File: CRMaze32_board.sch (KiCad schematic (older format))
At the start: 113 parts, among them IC101 L298, P101 CONN_01X02, P102 CONN_01X06, P103 CONN_01X06, P104 CONN_01X02, Q101 BFR92, Q102 BFR92, Q103 BFR92, Q104 BFR92, Q105 BFR92, SW101 SWITCH_INV, U101 LD1117S50TR, U102 74AHC1G14, U103 74AHC1G14, U104 LD1117S33TR, U105 ESP32-WROOM

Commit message: Placa CRMaze_board_futura con forma y componente colocados
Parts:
- removed 47K101, 47K102, 47K103, 47K104, 47K105, R105, R106, R110, R111, R114, R115, R? (x3): R, symbol R
- removed C101: 100n, symbol C
- removed C102: 10u, symbol C
- removed C103: 100n, Capacitors_SMD:C_0805_HandSoldering, symbol C
- removed C104: 10u, Capacitors_SMD:C_1206, symbol C
- removed D102, D107, D115, D116, D119, D120, D121, D122, D? (x3): LED, symbol LED
- removed D103, D104, D105, D106, D108, D109, D110, D111: D, diodos_smd:SMD_D_SMA-Sub-2, symbol D_Schottky
- removed IC101: L298, TO_SOT_Packages_THT:Multiwatt_15_Vertical, symbol L298
- removed P101: CONN_01X02, Pin_Headers:Pin_Header_Angled_1x02, symbol CONN_01X02
- removed P102, P103: CONN_01X06, Pin_Headers:Pin_Header_Straight_1x06, symbol CONN_01X06
- removed Q101, Q102, Q103, Q104, Q105: BFR92, symbol BFR92
- removed R101: 20k, symbol R
- removed R102: 10k, symbol R
- removed R103, R104: 0.5, Resistors_SMD:R_1206, symbol R
- removed SW101: SWITCH_INV, Buttons_Switches_SMD:SW_DIP_x4_W5.9mm_Slide_Copal_CVS, symbol SWITCH_INV
- removed U101: LD1117S50TR, symbol LD1117S50TR
- removed U102, U103: 74AHC1G14, symbol 74AHC1G14
- removed U104: LD1117S33TR, TO_SOT_Packages_SMD:SOT-223, symbol LD1117S33TR
- removed U?: ADXRS620_breakout, symbol ADXRS620_breakout
- removed U?: DRV8825_pololu, symbol DRV8825_pololu
- added J101, J102: CONN_01X02, Pin_Headers:Pin_Header_Angled_1x02, symbol CONN_01X02
- added P101: GYRO_ADXRS_2, Pin_Headers:Pin_Header_Straight_1x05, symbol CONN_01X05
- added P102: GYRO_ADXRS_1, Pin_Headers:Pin_Header_Straight_1x03, symbol CONN_01X03
- added P103: SERIAL, Pin_Headers:Pin_Header_Straight_1x03, symbol CONN_01X03
- added P105: ENC_1_POWER, Pin_Headers:Pin_Header_Straight_1x02, symbol CONN_01X02
- added P106: ENC_2_IN, Pin_Headers:Pin_Header_Straight_1x02, symbol CONN_01X02
- added P107: ENC_2_POWER, Pin_Headers:Pin_Header_Straight_1x02, symbol CONN_01X02
- added P108: MOTOR1, Pin_Headers:Pin_Header_Straight_1x02, symbol CONN_01X02
- added P109: MOTOR2, Pin_Headers:Pin_Header_Straight_1x02, symbol CONN_01X02
- added SW101: EN, Buttons_Switches_SMD:SW_SPST_EVQQ2, symbol SW_PUSH-RESCUE-CRMaze32_board
- added SW102: PUSH_IO_0, Buttons_Switches_SMD:SW_SPST_EVQQ2, symbol SW_PUSH-RESCUE-CRMaze32_board
- added SW103: SW_SPDT, switch:switch_power_custom, symbol SW_SPDT
- added U105: DRV8835_pololu, Housings_DIP:DIP-14_W7.62mm, symbol DRV8835_pololu
- 1.8k101: renamed from R107; footprint (none) -> Resistors_SMD:R_0805
- 1.8k102: renamed from R108; footprint (none) -> Resistors_SMD:R_0805
- 1.8k103: renamed from R109; footprint (none) -> Resistors_SMD:R_0805
- 1.8k104: renamed from R112; footprint (none) -> Resistors_SMD:R_0805
- 1.8k105: renamed from R113; footprint (none) -> Resistors_SMD:R_0805
- 1.8k106: renamed from R116; footprint (none) -> Resistors_SMD:R_0805
- 10ohm101, 10ohm102, 2.8ohm101, 2.8ohm102: renamed from R?; footprint (none) -> Resistors_SMD:R_1206
- 10uH101: renamed from 10uH; footprint (none) -> Capacitors_SMD:C_1206; symbol INDUCTOR -> INDUCTOR-RESCUE-CRMaze32_board
- 1k101, 1k102, 1k103, 1k104: renamed from R?; footprint (none) -> Resistors_SMD:R_0805
- BZ101: footprint (none) -> Capacitors_SMD:c_elec_4x5.8
- C101: renamed from C?; value C -> 100n; footprint (none) -> Capacitors_SMD:C_0805
- C102: renamed from C?; value C -> 10u; footprint (none) -> Capacitors_SMD:C_1206
- C103, C105, C108: renamed from C?; footprint (none) -> Capacitors_SMD:C_1206
- C104, C106, C107, C109: renamed from C?; footprint (none) -> Capacitors_SMD:C_0805
- C110, C112, C114: renamed from C?; value C -> 4.7uF; footprint (none) -> Capacitors_SMD:C_1206
- C111, C113, C115: renamed from C?; value C -> 100nF; footprint (none) -> Capacitors_SMD:C_0805
- D101, D114, D115, D116: renamed from D?; footprint (none) -> LEDs:LED-3MM; symbol LED -> LED-RESCUE-CRMaze32_board
- D102: renamed from D101; footprint (none) -> Diodes_SMD:D_0805
- D103: renamed from D112; value LED -> IR_DET; footprint (none) -> LEDs:LED-3MM; symbol LED -> LED-RESCUE-CRMaze32_board
- D104: renamed from D113; value LED -> IR_DET; footprint (none) -> LEDs:LED-3MM; symbol LED -> LED-RESCUE-CRMaze32_board
- D105, D107, D109, D110, D112, D113: renamed from D?; value LED -> IR_EMM; footprint (none) -> LEDs:LED-3MM; symbol LED -> LED-RESCUE-CRMaze32_board
- D106: renamed from D114; value LED -> IR_DET; footprint (none) -> LEDs:LED-3MM; symbol LED -> LED-RESCUE-CRMaze32_board
- D108: renamed from D117; value LED -> IR_DET; footprint (none) -> LEDs:LED-3MM; symbol LED -> LED-RESCUE-CRMaze32_board
- D111: renamed from D118; value LED -> IR_DET; footprint (none) -> LEDs:LED-3MM; symbol LED -> LED-RESCUE-CRMaze32_board
- D120: renamed from D123; value LED -> IR_DET; footprint (none) -> LEDs:LED-3MM; symbol LED -> LED-RESCUE-CRMaze32_board
- L101, L102, L103: renamed from L?; footprint (none) -> Capacitors_SMD:C_1206; symbol INDUCTOR -> INDUCTOR-RESCUE-CRMaze32_board
- P104: value CONN_01X02 -> ENC_1_IN; footprint Pin_Headers:Pin_Header_Angled_1x02 -> Pin_Headers:Pin_Header_Straight_1x02
- U102: renamed from U?; footprint (none) -> Housings_SOIC:SOIC-8-1EP_3.9x4.9mm_Pitch1.27mm
- U103: renamed from U?; footprint (none) -> TO_SOT_Packages_SMD:SOT-23-5
- U104: renamed from U?; footprint (none) -> Housings_SSOP:TSSOP-16_4.4x5mm_Pitch0.65mm; symbol ULN2003A -> ULN2003A-RESCUE-CRMaze32_board
- renumbered U105 to U101
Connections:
- net labels added: ENC_1_A, ENC_1_B, ENC_2_A, ENC_2_B
- net labels removed: +3.3V, +5V, CURRENT1, CURRENT2, ENC1_A, ENC1_B, ENC2_A, ENC2_B, GPIO_IR1, GPIO_IR23, GPIO_IR45, GPIO_IR6, GPIO_LED4, GPIO_LED5, GPIO_LED6, M1+, M1-, M2+, M2-, VCC, VDD, VOL_BAT
- wire segments 162 -> 147
- no-connect marks 3 -> 6
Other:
- note added: "ENCODERS"
- note removed: "A) LED IR EMMITER SYSTEM"
- note removed: "A) MOTOR DRIVER\n"
- note removed: "A) POWER SYSTEM CRMaze"
- moved on the sheet: 1.8k101, 1.8k102, 1.8k103, 1.8k104, 1.8k105, 1.8k106, 1k102, 1k103, 1k104, BZ101, C101, C102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

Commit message: retoques y moificaciones
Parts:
- removed P101: GYRO_ADXRS_2, Pin_Headers:Pin_Header_Straight_1x05, symbol CONN_01X05
- added J103: GYRO_ADXRS_2, Pin_Headers:Pin_Header_Straight_1x06, symbol CONN_01X06
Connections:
- wire segments 147 -> 145
- no-connect marks 6 -> 7
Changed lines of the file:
@@
 Text GLabel 2750 9250 1    60   Input ~ 0
 VA3.3
-Text GLabel 1650 10350 0    60   Input ~ 0
+Text GLabel 1600 10250 0    60   Input ~ 0
 GND
 Text GLabel 1900 9850 0    60   Input ~ 0
@@
 Text GLabel 5000 5150 3    60   Input ~ 0
 GPIO_LED1
+Text GLabel 5550 3450 2    60   Input ~ 0
+M1_EN
 Text GLabel 5550 3350 2    60   Input ~ 0
-M1_EN
-Text GLabel 5550 3450 2    60   Input ~ 0
 M1_DIR
 Text GLabel 5550 3750 2    60   Input ~ 0
@@
 	11350 2650 15650 2650
 Wire Wire Line
-	1750 10300 1950 10300
-Wire Wire Line
-	1750 10300 1750 10450
-Wire Wire Line
-	1750 10450 2050 10450
-Wire Wire Line
-	1650 10350 1750 10350
-Connection ~ 1750 10350
+	1700 10200 2150 10200
+Wire Wire Line
+	1700 10200 1700 10350
+Wire Wire Line
+	1700 10350 2000 10350
+Wire Wire Line
+	1600 10250 1700 10250
+Connection ~ 1700 10250
 Wire Notes Line
 	3700 10800 1200 10800
@@
 	0    1    1    0
 $EndComp
-$Comp
-L CONN_01X05 P101
-U 1 1 592C8D5B
-P 2350 10000
-F 0 "P101" H 2350 10300 50  0000 C CNN
-F 1 "GYRO_ADXRS_2" V 2450 10000 50  0000 C CNN
-F 2 "Pin_Headers:Pin_Header_Straight_1x05" H 2350 10000 50  0001 C CNN
-F 3 "" H 2350 10000 50  0000 C CNN
-	1    2350 10000
-	1    0    0    -1
-$EndComp
 Wire Wire Line
 	2150 9800 2050 9800
@@
 Wire Wire Line
 	1900 10000 2150 10000
-Wire Wire Line
-	1950 10300 1950 10100
-Wire Wire Line
-	1950 10100 2150 10100
-Wire Wire Line
-	2150 10200 2050 10200
-Wire Wire Line
-	2050 10200 2050 10450
 Wire Wire Line
 	2500 9250 2600 9250
@@
 Wire Wire Line
 	15400 3350 15400 3250
+$Comp
+L CONN_01X06 J103
+U 1 1 593738C8
+P 2350 10050
+F 0 "J103" H 2350 10400 50  0000 C CNN
+F 1 "GYRO_ADXRS_2" V 2450 10050 50  0000 C CNN
+F 2 "Pin_Headers:Pin_Header_Straight_1x06" H 2350 10050 50  0001 C CNN
+F 3 "" H 2350 10050 50  0001 C CNN
+	1    2350 10050
+	1    0    0    -1
+$EndComp
+Wire Wire Line
+	2150 10300 2000 10300
+Wire Wire Line
+	2000 10300 2000 10350
+NoConn ~ 2150 10100
 $EndSCHEMATC

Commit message: esquematico finalizado. Componentes colocados. Comienzo del enrutado.
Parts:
- removed U104: ULN2003A, Housings_SSOP:TSSOP-16_4.4x5mm_Pitch0.65mm, symbol ULN2003A-RESCUE-CRMaze32_board
- added 10ohm103, 10ohm104, R101, R102, R103, R104, R105, R106, R107: R, Resistors_SMD:R_0805, symbol R
- added Q101, Q102, Q103, Q104, Q105: BS107, TO_SOT_Packages_SMD:SOT-23, symbol BS107
- 10ohm101, 10ohm102: footprint Resistors_SMD:R_1206 -> Resistors_SMD:R_0805
- 10ohm121: renamed from 2.8ohm101; footprint Resistors_SMD:R_1206 -> Resistors_SMD:R_0805
- 10ohm122: renamed from 2.8ohm102; footprint Resistors_SMD:R_1206 -> Resistors_SMD:R_0805
- 10uH101, L101, L102, L103: footprint Capacitors_SMD:C_1206 -> Inductors_SMD:L_0805
- D114, D115, D116: footprint LEDs:LED-3MM -> LEDs:LED_1206
- SW101, SW102: footprint Buttons_Switches_SMD:SW_SPST_EVQQ2 -> ESP32-footprints-Lib:smd_button
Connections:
- net ENC_2_B: now also U101.37 (IO23); no longer U101.14 (IO12)
- net GND: now also C104.2, Q101.3 (S), Q102.3 (S), Q103.3 (S), Q104.3 (S), Q105.3 (S)
- net GPIO_BUZZER: now also R101.2
- net GPIO_IR_DIAG: now also R104.2
- net GPIO_IR_FL: now also R102.2
- net GPIO_IR_FR: now also R103.2
- net GPIO_IR_SIDE: now also U101.31 (IO19), R105.2; no longer U101.29 (IO5)
- net M1_DIR: now also U101.14 (IO12); no longer U101.37 (IO23)
- net M2_DIR: now also U101.29 (IO5); no longer U101.31 (IO19)
- net V3.3: now also R106.2, R107.1
- net at SW101.2, U101.3 (EN): now also R106.1
- net at 10ohm102.2: now also 10ohm104.2, Q105.1 (D)
- net at 10ohm122.2: now also Q103.1 (D)
- net at 10ohm121.2: now also Q102.1 (D)
- net at 10ohm101.2: now also 10ohm103.2, Q104.1 (D)
- net at 10ohm101.1, D110.1 (K): now also 10ohm103.1
- net at 10ohm102.1, D113.1 (K): now also 10ohm104.1
- net BUZZER_CONTROL: no longer names the net of BZ101.2, D102.2 (A)
- net BUZZER_CONTROL: now also Q101.1 (D), R107.2
- new net: Q102.2 (G), R102.1
- new net: Q103.2 (G), R103.1
- new net: Q104.2 (G), R104.1
- new net: Q105.2 (G), R105.1
- new net: Q101.2 (G), R101.1
- no-connect marks 7 -> 6
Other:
- note added: "(DOWN)"
- note added: "(UP)"
- note added: "Cambiar el footprint a uno modificado a mano por Carlos"
- note added: "Footprint 0805"
- note added: "Footprint 1206 (verde/rojo) o 0603"
- note added: "footprint 0805"
- moved on the sheet: 10ohm121, 10ohm122, D105, D107

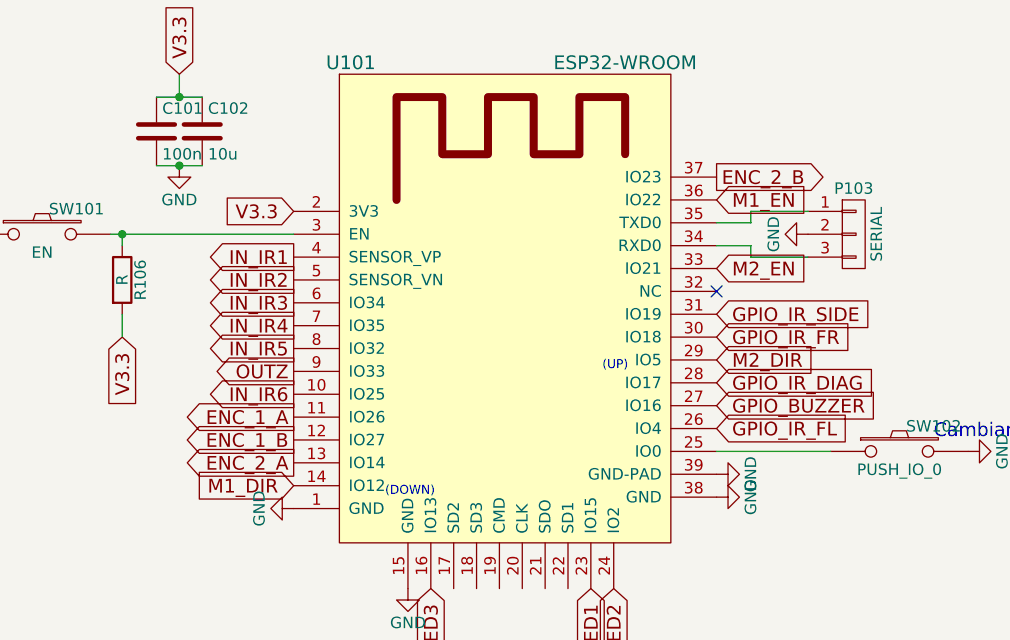
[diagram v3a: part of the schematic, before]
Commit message: avances enrutado
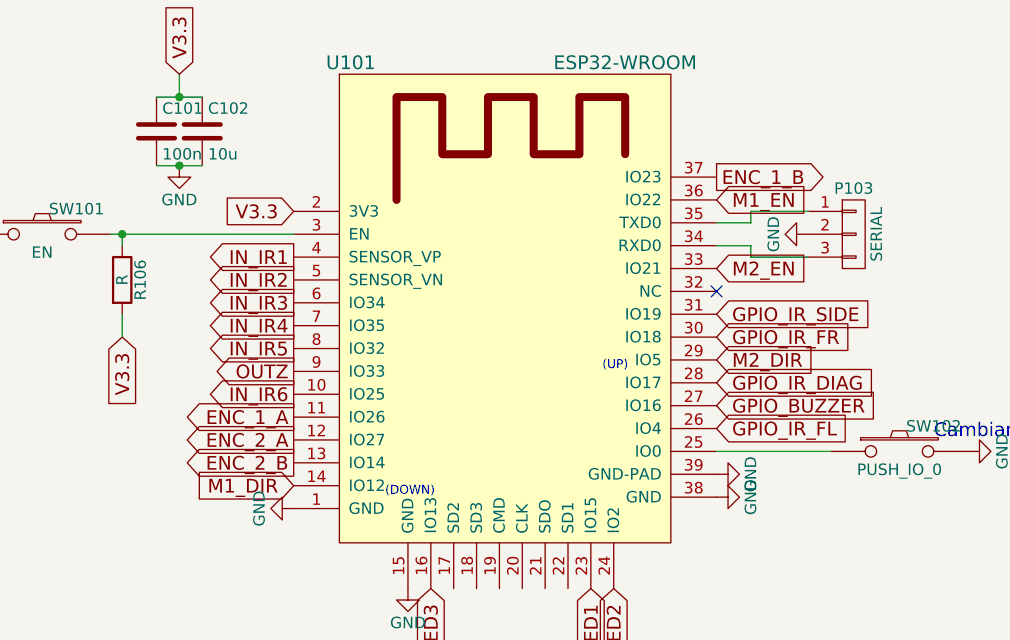
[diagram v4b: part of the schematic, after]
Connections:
- net ENC_1_B: now also U101.37 (IO23); no longer U101.12 (IO27)
- net ENC_2_A: now also U101.12 (IO27); no longer U101.13 (IO14)
- net ENC_2_B: now also U101.13 (IO14); no longer U101.37 (IO23)
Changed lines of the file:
@@
 Text GLabel 3700 4400 0    60   Output ~ 0
 ENC_1_A
+Text GLabel 5550 3350 2    60   Output ~ 0
+ENC_1_B
 Text GLabel 3700 4500 0    60   Output ~ 0
-ENC_1_B
+ENC_2_A
 Text GLabel 3700 4600 0    60   Output ~ 0
-ENC_2_A
-Text GLabel 5550 3350 2    60   Output ~ 0
 ENC_2_B
 NoConn ~ 5550 3850

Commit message: pre cambio etiquetas esquematico
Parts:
- renumbered 10uH101 to L101
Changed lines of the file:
@@
 $EndComp
 $Comp
-L INDUCTOR-RESCUE-CRMaze32_board 10uH101
+L INDUCTOR-RESCUE-CRMaze32_board L101
 U 1 1 58D6DD1D
 P 7500 8950
-F 0 "10uH101" V 7450 8950 50  0000 C CNN
+F 0 "L101" V 7450 8950 50  0000 C CNN
 F 1 "INDUCTOR" V 7600 8950 50  0000 C CNN
 F 2 "Inductors_SMD:L_0805" H 7500 8950 50  0001 C CNN
@@
 AGND
 $Comp
-L GND #PWR01
+L GND #PWR109
 U 1 1 58D906D9
 P 7200 10350
-F 0 "#PWR01" H 7200 10100 50  0001 C CNN
+F 0 "#PWR109" H 7200 10100 50  0001 C CNN
 F 1 "GND" H 7200 10200 50  0000 C CNN
 F 2 "" H 7200 10350 50  0000 C CNN
@@
 GPIO_LED1
 $Comp
-L GND #PWR02
+L GND #PWR118
 U 1 1 58D96097
 P 15500 4600
-F 0 "#PWR02" H 15500 4350 50  0001 C CNN
+F 0 "#PWR118" H 15500 4350 50  0001 C CNN
 F 1 "GND" H 15500 4450 50  0000 C CNN
 F 2 "" H 15500 4600 50  0000 C CNN
@@
 GPIO_LED2
 $Comp
-L GND #PWR03
+L GND #PWR119
 U 1 1 58D964E8
 P 15500 4900
-F 0 "#PWR03" H 15500 4650 50  0001 C CNN
+F 0 "#PWR119" H 15500 4650 50  0001 C CNN
 F 1 "GND" H 15500 4750 50  0000 C CNN
 F 2 "" H 15500 4900 50  0000 C CNN
@@
 GPIO_LED3
 $Comp
-L GND #PWR04
+L GND #PWR120
 U 1 1 58D96611
 P 15500 5200
-F 0 "#PWR04" H 15500 4950 50  0001 C CNN
+F 0 "#PWR120" H 15500 4950 50  0001 C CNN
 F 1 "GND" H 15500 5050 50  0000 C CNN
 F 2 "" H 15500 5200 50  0000 C CNN
@@
 MODE INDICATION SYSTEM
 $Comp
-L GND #PWR05
+L GND #PWR106
 U 1 1 592B68D4
 P 5550 4750
-F 0 "#PWR05" H 5550 4500 50  0001 C CNN
+F 0 "#PWR106" H 5550 4500 50  0001 C CNN
 F 1 "GND" H 5550 4600 50  0000 C CNN
 F 2 "" H 5550 4750 50  0000 C CNN
@@
 $EndComp
 $Comp
-L GND #PWR06
+L GND #PWR105
 U 1 1 592B69A3
 P 5550 4650
-F 0 "#PWR06" H 5550 4400 50  0001 C CNN
+F 0 "#PWR105" H 5550 4400 50  0001 C CNN
 F 1 "GND" H 5550 4500 50  0000 C CNN
 F 2 "" H 5550 4650 50  0000 C CNN
@@
 $EndComp
 $Comp
-L GND #PWR07
+L GND #PWR104
 U 1 1 592B6A6B
 P 4200 5150
-F 0 "#PWR07" H 4200 4900 50  0001 C CNN
+F 0 "#PWR104" H 4200 4900 50  0001 C CNN
 F 1 "GND" H 4200 5000 50  0000 C CNN
 F 2 "" H 4200 5150 50  0000 C CNN
@@
 $EndComp
 $Comp
-L GND #PWR08
+L GND #PWR103
 U 1 1 592B6B33
 P 3700 4800
-F 0 "#PWR08" H 3700 4550 50  0001 C CNN
+F 0 "#PWR103" H 3700 4550 50  0001 C CNN
 F 1 "GND" H 3700 4650 50  0000 C CNN
 F 2 "" H 3700 4800 50  0000 C CNN
@@
 $EndComp
 $Comp
-L GND #PWR09
+L GND #PWR108
 U 1 1 592B77CD
 P 6650 4550
-F 0 "#PWR09" H 6650 4300 50  0001 C CNN
+F 0 "#PWR108" H 6650 4300 50  0001 C CNN
 F 1 "GND" H 6650 4400 50  0000 C CNN
 F 2 "" H 6650 4550 50  0000 C CNN
@@
 $EndComp
 $Comp
-L GND #PWR010
+L GND #PWR107
 U 1 1 592B7B38
 P 5950 3600
-F 0 "#PWR010" H 5950 3350 50  0001 C CNN
+F 0 "#PWR107" H 5950 3350 50  0001 C CNN
 F 1 "GND" H 5950 3450 50  0000 C CNN
 F 2 "" H 5950 3600 50  0000 C CNN
@@
 V3.3
 $Comp
-L GND #PWR011
+L GND #PWR102
 U 1 1 592B8BA7
 P 3200 3300
-F 0 "#PWR011" H 3200 3050 50  0001 C CNN
+F 0 "#PWR102" H 3200 3050 50  0001 C CNN
 F 1 "GND" H 3200 3150 50  0000 C CNN
 F 2 "" H 3200 3300 50  0000 C CNN
@@
 $EndComp
 $Comp
-L GND #PWR012
+L GND #PWR101
 U 1 1 592BD8A7
 P 2300 3600
-F 0 "#PWR012" H 2300 3350 50  0001 C CNN
+F 0 "#PWR101" H 2300 3350 50  0001 C CNN
 F 1 "GND" H 2300 3450 50  0000 C CNN
 F 2 "" H 2300 3600 50  0000 C CNN
@@
 V3.3
 $Comp
-L GND #PWR013
+L GND #PWR111
 U 1 1 592C038C
 P 11700 6750
-F 0 "#PWR013" H 11700 6500 50  0001 C CNN
+F 0 "#PWR111" H 11700 6500 50  0001 C CNN
 F 1 "GND" H 11700 6600 50  0000 C CNN
 F 2 "" H 11700 6750 50  0000 C CNN
@@
 $EndComp
 $Comp
-L GND #PWR014
+L GND #PWR114
 U 1 1 592C0470
 P 12700 6700
-F 0 "#PWR014" H 12700 6450 50  0001 C CNN
+F 0 "#PWR114" H 12700 6450 50  0001 C CNN
 F 1 "GND" H 12700 6550 50  0000 C CNN
 F 2 "" H 12700 6700 50  0000 C CNN
@@
 GPIO_IR_DIAG
 $Comp
-L GND #PWR015
+L GND #PWR112
 U 1 1 593AFFCB
 P 11750 1200
-F 0 "#PWR015" H 11750 950 50  0001 C CNN
+F 0 "#PWR112" H 11750 950 50  0001 C CNN
 F 1 "GND" H 11750 1050 50  0000 C CNN
 F 2 "" H 11750 1200 50  0001 C CNN
@@
 $EndComp
 $Comp
-L GND #PWR016
+L GND #PWR113
 U 1 1 593B16C9
 P 12000 1550
-F 0 "#PWR016" H 12000 1300 50  0001 C CNN
+F 0 "#PWR113" H 12000 1300 50  0001 C CNN
 F 1 "GND" H 12000 1400 50  0000 C CNN
 F 2 "" H 12000 1550 50  0001 C CNN
@@
 $EndComp
 $Comp
-L GND #PWR017
+L GND #PWR115
 U 1 1 593B2A55
 P 12750 1900
-F 0 "#PWR017" H 12750 1650 50  0001 C CNN
+F 0 "#PWR115" H 12750 1650 50  0001 C CNN
 F 1 "GND" H 12750 1750 50  0000 C CNN
 F 2 "" H 12750 1900 50  0001 C CNN
@@
 $EndComp
 $Comp
-L GND #PWR018
+L GND #PWR117
 U 1 1 593B480E
 P 15450 2300
-F 0 "#PWR018" H 15450 2050 50  0001 C CNN
+F 0 "#PWR117" H 15450 2050 50  0001 C CNN
 F 1 "GND" H 15450 2150 50  0000 C CNN
 F 2 "" H 15450 2300 50  0001 C CNN
@@
 $EndComp
 $Comp
-L GND #PWR019
+L GND #PWR116
 U 1 1 593B4D4B
 P 13050 2300
-F 0 "#PWR019" H 13050 2050 50  0001 C CNN
+F 0 "#PWR116" H 13050 2050 50  0001 C CNN
 F 1 "GND" H 13050 2150 50  0000 C CNN
 F 2 "" H 13050 2300 50  0001 C CNN
@@
 $EndComp
 $Comp
-L GND #PWR020
+L GND #PWR110
 U 1 1 593B569A
 P 8550 2000
-F 0 "#PWR020" H 8550 1750 50  0001 C CNN
+F 0 "#PWR110" H 8550 1750 50  0001 C CNN
 F 1 "GND" H 8550 1850 50  0000 C CNN
 F 2 "" H 8550 2000 50  0001 C CNN
